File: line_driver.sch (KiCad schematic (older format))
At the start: 30 parts, among them J8 DRV632

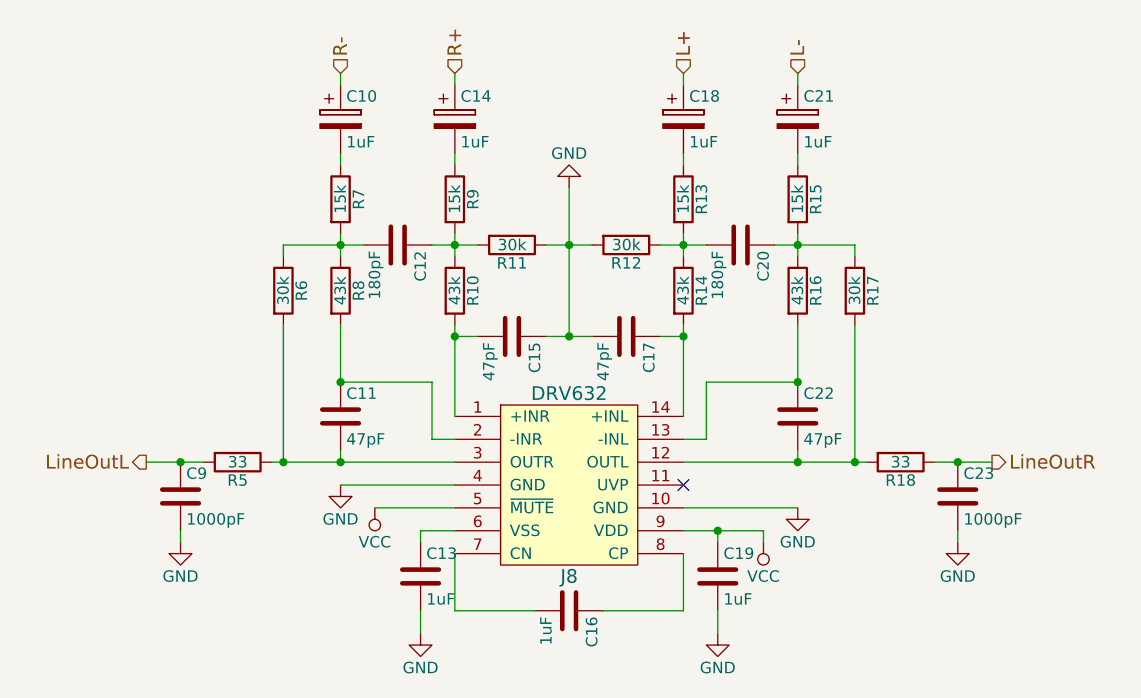
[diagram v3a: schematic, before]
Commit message: Reduce the line driver back to simple
After determining the gain needed to be 0.735 (which is out of spec for
the amp), I was unsure what to do with the 2nd order filter on the amp.
It wasn't even present on the headphone amp from before, and I suspect
the head unit in the car does some filtering of its own. To simplify
things, I removed the second order filter and went back to a simple line
driver. I also set the values of the gain setting resistors to 8.2 and
11, which gets as close as I can to 0.735 gain using single E24
resistors.
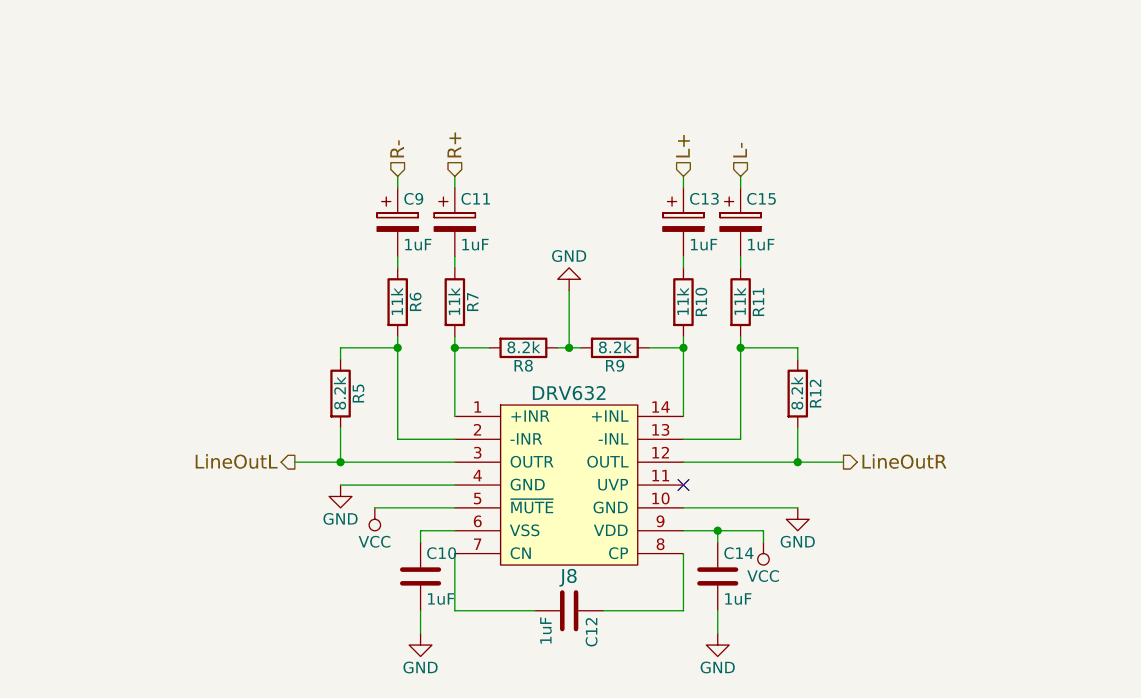
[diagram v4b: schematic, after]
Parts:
- removed C10, C14, C18, C21: 1uF, blubaru:CP_Radial_D4.0mm_P1.50mm, symbol CP
- removed C11, C15, C17, C22: 47pF, blubaru:C_Disc_D4.0mm_W2.6mm_P2.50mm, symbol C
- removed C12, C20: 180pF, blubaru:C_Disc_D4.0mm_W2.6mm_P2.50mm, symbol C
- removed C23, C9: 1000pF, blubaru:C_Disc_D4.0mm_W2.6mm_P2.50mm, symbol C
- removed R10, R14, R16, R8: 43k, Resistors_THT:R_Axial_DIN0204_L3.6mm_D1.6mm_P5.08mm_Horizontal, symbol R
- removed R18, R5: 33, Resistors_THT:R_Axial_DIN0204_L3.6mm_D1.6mm_P5.08mm_Horizontal, symbol R
- added C11, C13, C15, C9: 1uF, blubaru:CP_Radial_D4.0mm_P1.50mm, symbol CP
- R10: renamed from R13; value 15k -> 11k
- R11: renamed from R15; value 15k -> 11k
- R12: renamed from R17; value 30k -> 8.2k
- R5: renamed from R6; value 30k -> 8.2k
- R6: renamed from R7; value 15k -> 11k
- R7: renamed from R9; value 15k -> 11k
- R8: renamed from R11; value 30k -> 8.2k
- R9: renamed from R12; value 30k -> 8.2k
- renumbered C13 to C10, C16 to C12, C19 to C14
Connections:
- net L+: now also C13.1
- net L-: now also C15.1
- net LineOutL: now also J8.3 (OUTR), R5.2
- net LineOutR: now also J8.12 (OUTL), R12.2
- net R+: now also C11.1
- net R-: now also C9.1
- net at J8.13 (-INL): now also R11.2, R12.1
- net at J8.2 (-INR): now also R5.1, R6.2
- net at J8.14 (+INL): now also R10.2, R9.1
- net at J8.1 (+INR): now also R7.2, R8.2
- net at R10.1: now also C13.2
- net at R7.1: now also C11.2
- net at R11.1: now also C15.2
- net at R6.1: now also C9.2
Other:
- moved on the sheet: R10, R11, R12, R5, R6, R7, R8, R9

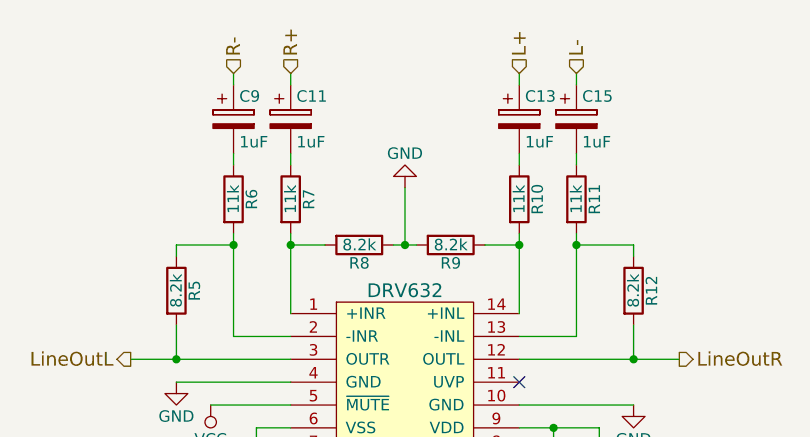
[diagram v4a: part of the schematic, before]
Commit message: Separate audio ground from power ground
The connection between the CD player and stereo has a separate line for
audio ground and the chassis ground. I didn't previously understand why
this was necessary, so I tied them together. They were tied together in
the stereo anyway. The reason is that when using power, there must be
current returning on the ground line, and since that ground line is not
free of resistance, that causes a slight voltage change. That voltage
difference causes a disagreement in what ground is, and at audio levels,
that makes a significant difference. By isolating the audio ground to a
separate wire that doesn't carry current, we keep the ground potential
the same between the devices, and the audio comes out much cleaner.

On the main connector, I've kept the chassis ground as the power ground,
and only connected the audio ground to the mid-rail on the line driver,
and the line-in ground, as those are the places where audio ground
potential will matter.

As I now understand the grounding situation better, I'm removing the
ground jumper pads.

I will also consider removing the voltage regulator if I can get enough
power out of the regulator on board with the MCU.
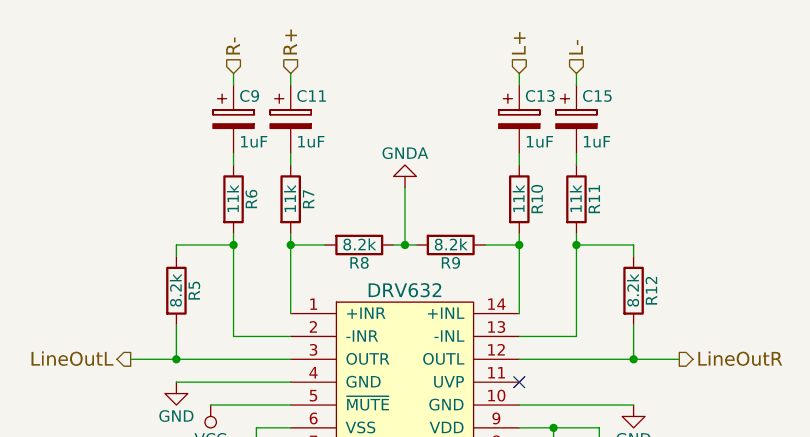
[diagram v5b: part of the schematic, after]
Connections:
- net GND: no longer R8.1, R9.2
- new net GNDA: R8.1, R9.2
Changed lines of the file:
@@
-$EndComp
-$Comp
-L GND #PWR034
-U 1 1 5917926C
-P 5800 2550
-F 0 "#PWR034" H 5800 2300 50  0001 C CNN
-F 1 "GND" H 5800 2400 50  0000 C CNN
-F 2 "" H 5800 2550 50  0001 C CNN
-F 3 "" H 5800 2550 50  0001 C CNN
-	1    5800 2550
-	-1   0    0    1
 $EndComp
 $Comp
@@
 	1    0    0    -1
 $EndComp
+$Comp
+L GNDA #PWR034
+U 1 1 59C097AE
+P 5800 2550
+F 0 "#PWR034" H 5800 2300 50  0001 C CNN
+F 1 "GNDA" H 5800 2400 50  0000 C CNN
+F 2 "" H 5800 2550 50  0000 C CNN
+F 3 "" H 5800 2550 50  0000 C CNN
+	1    5800 2550
+	-1   0    0    1
+$EndComp
 $EndSCHEMATC
